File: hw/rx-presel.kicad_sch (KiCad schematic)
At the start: 55 parts, among them U1501 SN74LVC04APW, U1502 SN74LVC04APW, U1503 AS183-92LF, U1504 MCP23S17, U1505 AS183-92LF, U1506 AS183-92LF, U1507 AS183-92LF, U1508 AS183-92LF, U1509 AS183-92LF, U1510 AS183-92LF, U1511 AS183-92LF, U1512 AS183-92LF, U1513 AS183-92LF, U1514 AS183-92LF, U1515 AS183-92LF

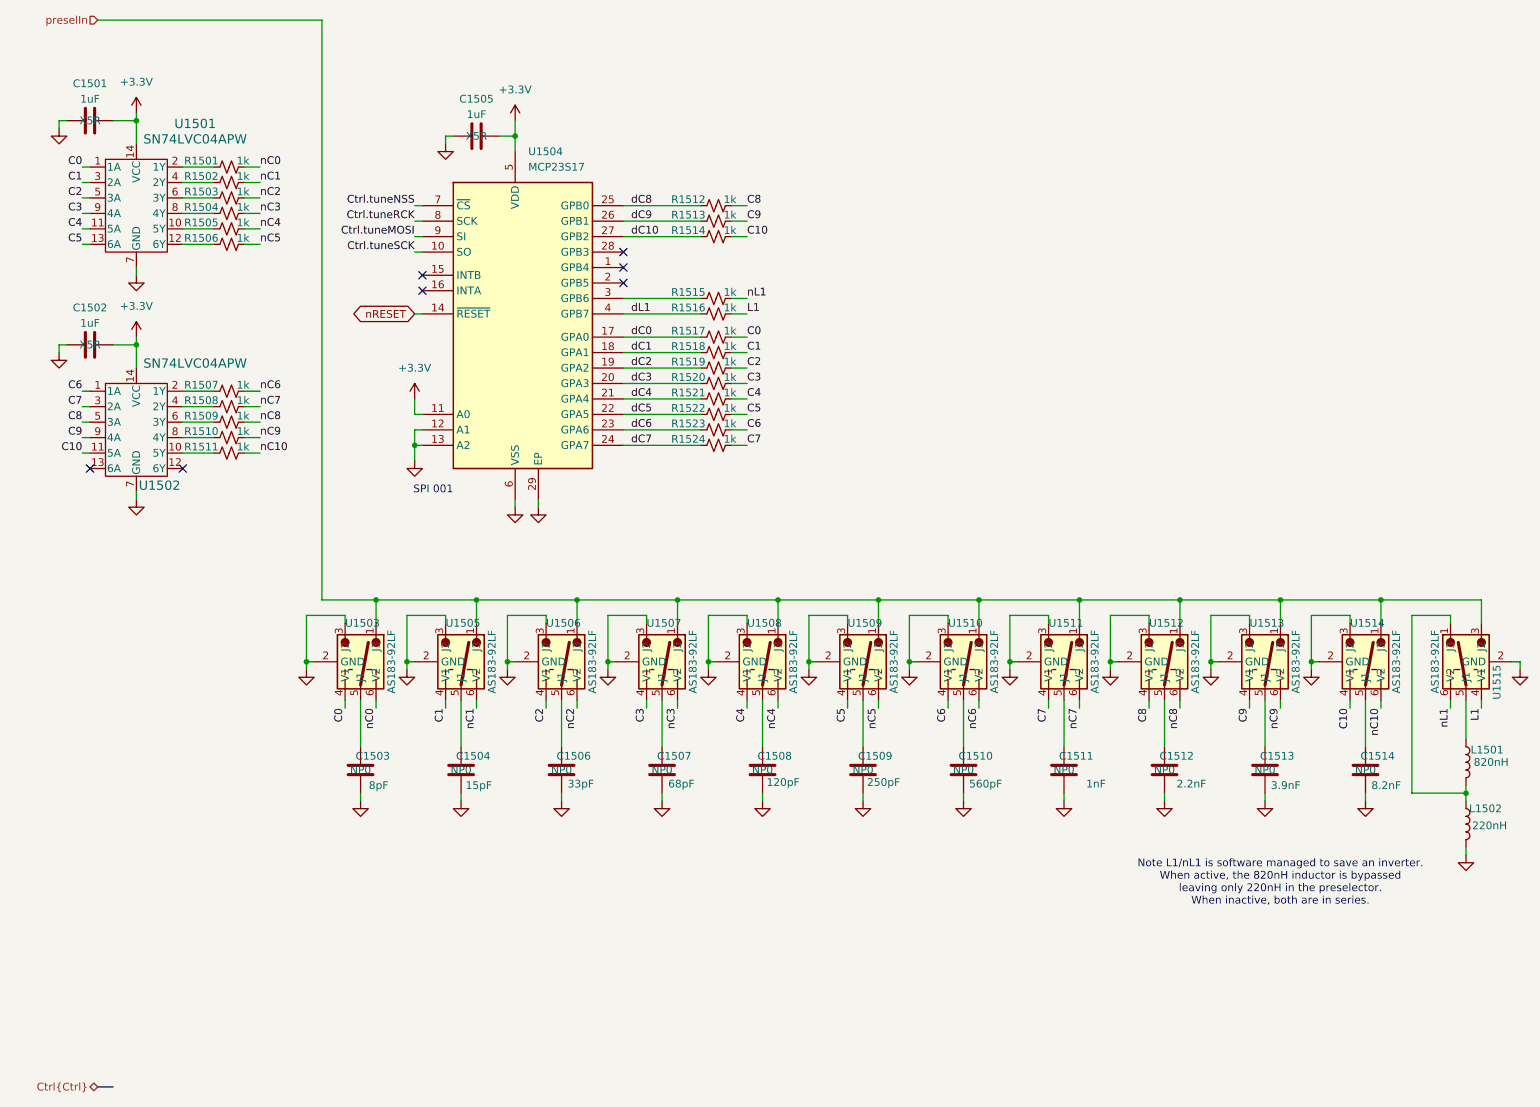
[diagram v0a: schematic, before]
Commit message: Checkpoint. Now using TQFP100 STM32H753VIT6, no longer using SPI expanders to drive controls for L,C,atten. FPGA does that now.
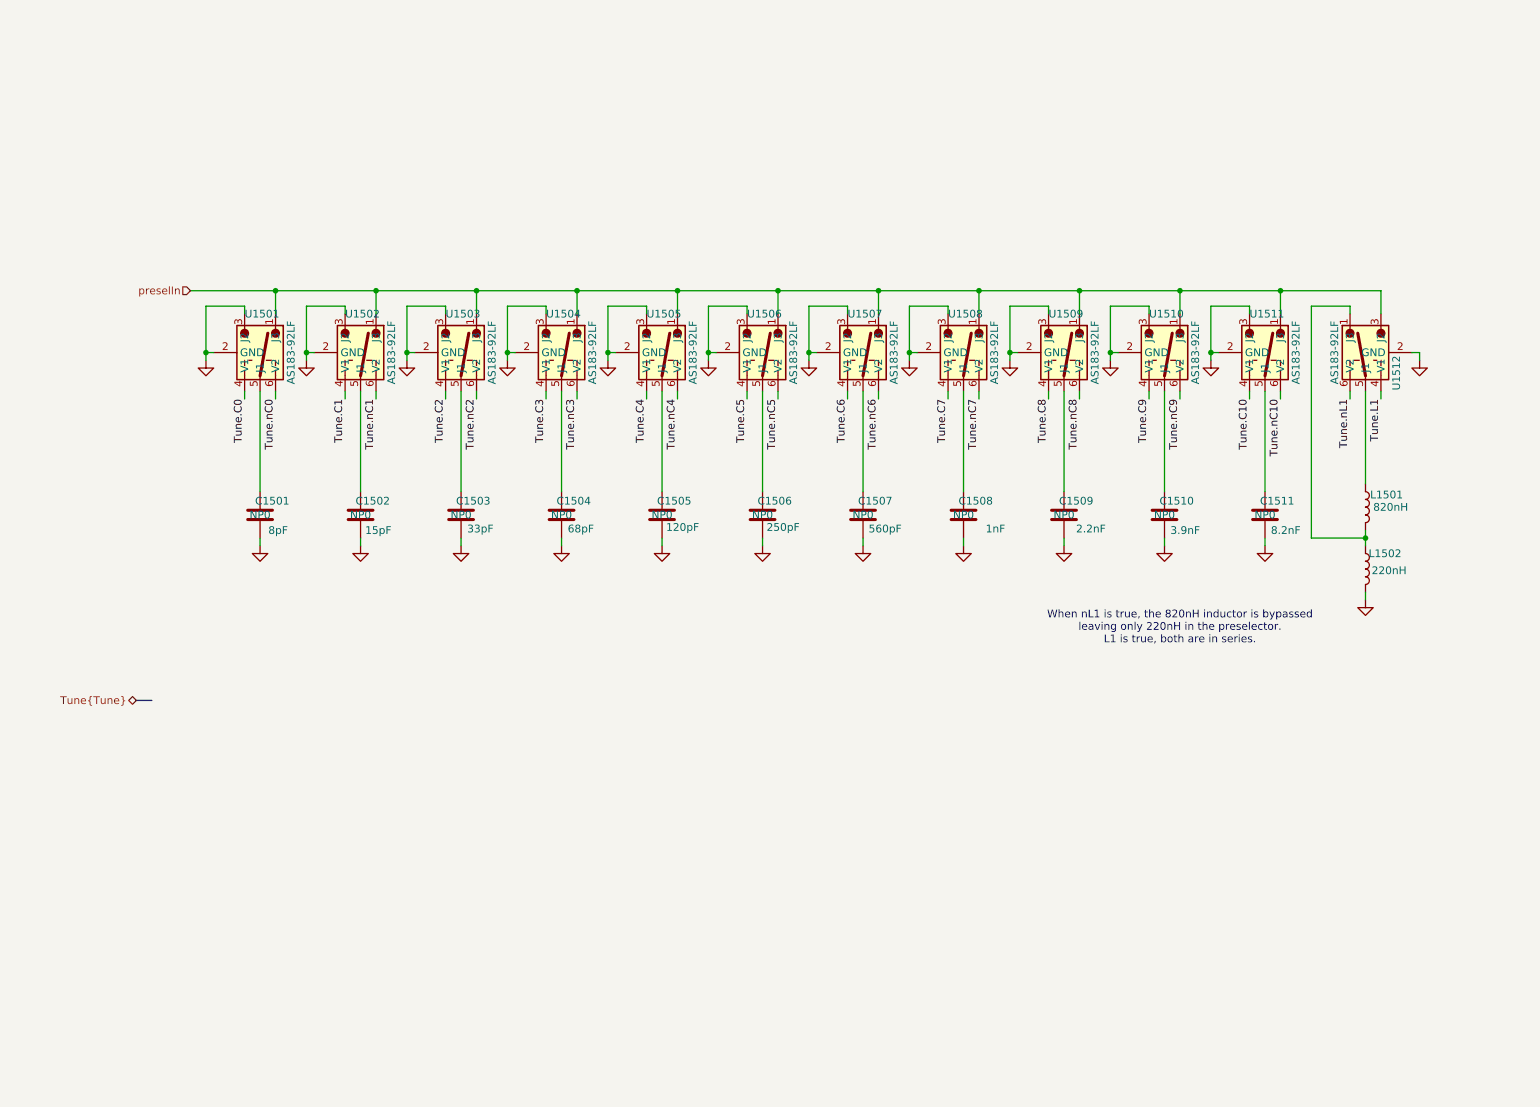
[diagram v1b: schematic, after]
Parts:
- removed C1501, C1502, C1505: 1uF, Capacitor_SMD:C_0402_1005Metric, symbol Device:C
- removed R1501, R1502, R1503, R1504, R1505, R1506, R1507, R1508, R1509, R1510, R1511, R1512, R1513, R1514, R1515, R1516, R1517, R1518, R1519, R1520, R1521, R1522, R1523, R1524: 1k, Resistor_SMD:R_0402_1005Metric, symbol Device:R_Small_US
- removed U1501, U1502: SN74LVC04APW, Library:PW14, symbol Library:SN74LVC04APW
- removed U1504: MCP23S17, Library:QFN65P600X600X100-29N-D, symbol Library:MCP23S17T-E_ML
- renumbered C1503 to C1501, C1504 to C1502, C1506 to C1503, C1507 to C1504, C1508 to C1505, C1509 to C1506, C1510 to C1507, C1511 to C1508, C1512 to C1509, C1513 to C1510, C1514 to C1511, U1503 to U1501, U1505 to U1502, U1506 to U1503, U1507 to U1504, U1508 to U1505, U1509 to U1506, U1510 to U1507, U1511 to U1508, U1512 to U1509, U1513 to U1510, U1514 to U1511, U1515 to U1512
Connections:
- net C0 renamed Tune.C0
- net C1 renamed Tune.C1
- net C10 renamed Tune.C10
- net C2 renamed Tune.C2
- net C3 renamed Tune.C3
- net C4 renamed Tune.C4
- net C5 renamed Tune.C5
- net C6 renamed Tune.C6
- net C7 renamed Tune.C7
- net C8 renamed Tune.C8
- net C9 renamed Tune.C9
- net L1 renamed Tune.L1
- net nC0 renamed Tune.nC0
- net nC1 renamed Tune.nC1
- net nC10 renamed Tune.nC10
- net nC2 renamed Tune.nC2
- net nC3 renamed Tune.nC3
- net nC4 renamed Tune.nC4
- net nC5 renamed Tune.nC5
- net nC6 renamed Tune.nC6
- net nC7 renamed Tune.nC7
- net nC8 renamed Tune.nC8
- net nC9 renamed Tune.nC9
- net nL1 renamed Tune.nL1
- no-connect marks 7 -> 0
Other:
- note added: "When nL1 is true, the 820nH inductor is bypassed leaving only 220nH in the preselector. L1 is true, both are in series."
- note removed: "Note L1/nL1 is software managed to save an inverter. When active, the 820nH inductor is bypassed leaving only 220nH in the preselector. When inactive, both are in series."
- note removed: "SPI 001"
- moved on the sheet: C1501, C1502, C1503, C1504, C1505, C1506, C1507, C1508, C1509, C1510, C1511, L1501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

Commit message: Starting to think about routing
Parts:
- L701: renamed from L1501; value 820nH -> 1.5uH; symbol Device:L -> Device:L_Ferrite_Small; MP NLV32T-8R2J-EF -> NLV32T-1R5J-EF; Mouser-part-number (none) -> 810-NLV32T-1R5J-EF
- L702: renamed from L1502; symbol Device:L -> Device:L_Ferrite_Small
- renumbered C1501 to C701, C1502 to C702, C1503 to C703, C1504 to C704, C1505 to C705, C1506 to C706, C1507 to C707, C1508 to C708, C1509 to C709, C1510 to C710, C1511 to C711, U1501 to U701, U1502 to U702, U1503 to U703, U1504 to U704, U1505 to U705, U1506 to U706, U1507 to U707, U1508 to U708, U1509 to U709, U1510 to U710, U1511 to U711, U1512 to U712
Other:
- note added: "When nL1 is true, the 1.5uH inductor is bypassed leaving only 220nH in the preselector. L1 is true, both are in series."
- note removed: "When nL1 is true, the 820nH inductor is bypassed leaving only 220nH in the preselector. L1 is true, both are in series."

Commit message: checkpoint
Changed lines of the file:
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@@
 	(wire
 		(pts
+			(xy 242.57 76.2) (xy 243.84 76.2)
+		)
+		(stroke
+			(width 0)
+			(type default)
+		)
+	)
+	(wire
+		(pts
 			(xy 215.9 82.55) (xy 215.9 83.82)
 		)
@@
 	(wire
 		(pts
-			(xy 243.84 76.2) (xy 243.84 77.47)
-		)
-		(stroke
-			(width 0)
-			(type default)
-		)
-	)
-	(wire
-		(pts
 			(xy 77.47 77.47) (xy 77.47 76.2)
 		)
@@
 	(wire
 		(pts
+			(xy 243.84 76.2) (xy 243.84 77.47)
+		)
+		(stroke
+			(width 0)
+			(type default)
+		)
+	)
+	(wire
+		(pts
 			(xy 121.92 82.55) (xy 121.92 83.82)
 		)
@@
 	(wire
 		(pts
-			(xy 243.84 76.2) (xy 242.57 76.2)
-		)
-		(stroke
-			(width 0)
-			(type default)
-		)
-	)
-	(wire
-		(pts
 			(xy 204.47 82.55) (xy 204.47 83.82)
 		)
@@
 		(lib_id "power:GND")
 		(at 243.84 77.47 0)
+		(mirror y)
 		(unit 1)
 		(exclude_from_sim no)

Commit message: Checkpoint to prep for full scale Gemini review and cleanup
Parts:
- U701, U702, U703, U704, U705, U706, U707, U708, U709, U710, U711, U712: JCLPCBpn (none) -> C53413616; Manufacturer_Part_Number AS183-92LF -> AS183-92LF-HX

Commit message: hw: change AS183-92LF-HX to AS183-92LF and update T301 description
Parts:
- U701, U702, U703, U704, U705, U706, U707, U708, U709, U710, U711, U712: Manufacturer_Part_Number AS183-92LF-HX -> AS183-92LF
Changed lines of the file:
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@@
 			)
 		)
-		(property "Manufacturer_Part_Number" "AS183-92LF-HX"
+		(property "Manufacturer_Part_Number" "AS183-92LF"
 			(at 1029.87 97.79 0)
 			(effects
@@
 			)
 		)
-		(property "Manufacturer_Part_Number" "AS183-92LF-HX"
+		(property "Manufacturer_Part_Number" "AS183-92LF"
 			(at -592.99 97.79 0)
 			(effects
@@
 			)
 		)
-		(property "Manufacturer_Part_Number" "AS183-92LF-HX"
+		(property "Manufacturer_Part_Number" "AS183-92LF"
 			(at -659.03 97.79 0)
 			(effects
@@
 			)
 		)
-		(property "Manufacturer_Part_Number" "AS183-92LF-HX"
+		(property "Manufacturer_Part_Number" "AS183-92LF"
 			(at -642.52 97.79 0)
 			(effects
@@
 			)
 		)
-		(property "Manufacturer_Part_Number" "AS183-92LF-HX"
+		(property "Manufacturer_Part_Number" "AS183-92LF"
 			(at -675.54 97.79 0)
 			(effects
@@
 			)
 		)
-		(property "Manufacturer_Part_Number" "AS183-92LF-HX"
+		(property "Manufacturer_Part_Number" "AS183-92LF"
 			(at -741.58 97.79 0)
 			(effects
@@
 			)
 		)
-		(property "Manufacturer_Part_Number" "AS183-92LF-HX"
+		(property "Manufacturer_Part_Number" "AS183-92LF"
 			(at -609.5 97.79 0)
 			(effects
@@
 			)
 		)
-		(property "Manufacturer_Part_Number" "AS183-92LF-HX"
+		(property "Manufacturer_Part_Number" "AS183-92LF"
 			(at -626.01 97.79 0)
 			(effects
@@
 			)
 		)
-		(property "Manufacturer_Part_Number" "AS183-92LF-HX"
+		(property "Manufacturer_Part_Number" "AS183-92LF"
 			(at -576.48 97.79 0)
 			(effects
@@
 			)
 		)
-		(property "Manufacturer_Part_Number" "AS183-92LF-HX"
+		(property "Manufacturer_Part_Number" "AS183-92LF"
 			(at -708.56 97.79 0)
 			(effects
@@
 			)
 		)
-		(property "Manufacturer_Part_Number" "AS183-92LF-HX"
+		(property "Manufacturer_Part_Number" "AS183-92LF"
 			(at -692.05 97.79 0)
 			(effects
@@
 			)
 		)
-		(property "Manufacturer_Part_Number" "AS183-92LF-HX"
+		(property "Manufacturer_Part_Number" "AS183-92LF"
 			(at -725.07 97.79 0)
 			(effects

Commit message: hw: remove ethernet page (page 24) and sync BOM metadata
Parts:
- L701: JLCPCBpn (none) -> C286756
- L702: JLCPCBpn (none) -> C295117
- U701, U702, U703, U704, U705, U706, U707, U708, U709, U710, U711, U712: JCLPCBpn C53413616 -> (none); JLCPCBpn (none) -> C2654768
